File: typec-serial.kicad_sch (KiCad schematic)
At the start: 16 parts, among them IC1 NJM12888F33-TE1, J1 USB4085-GF-A_REVB, J2 Conn_01x04_Pin, U1 FT230XS

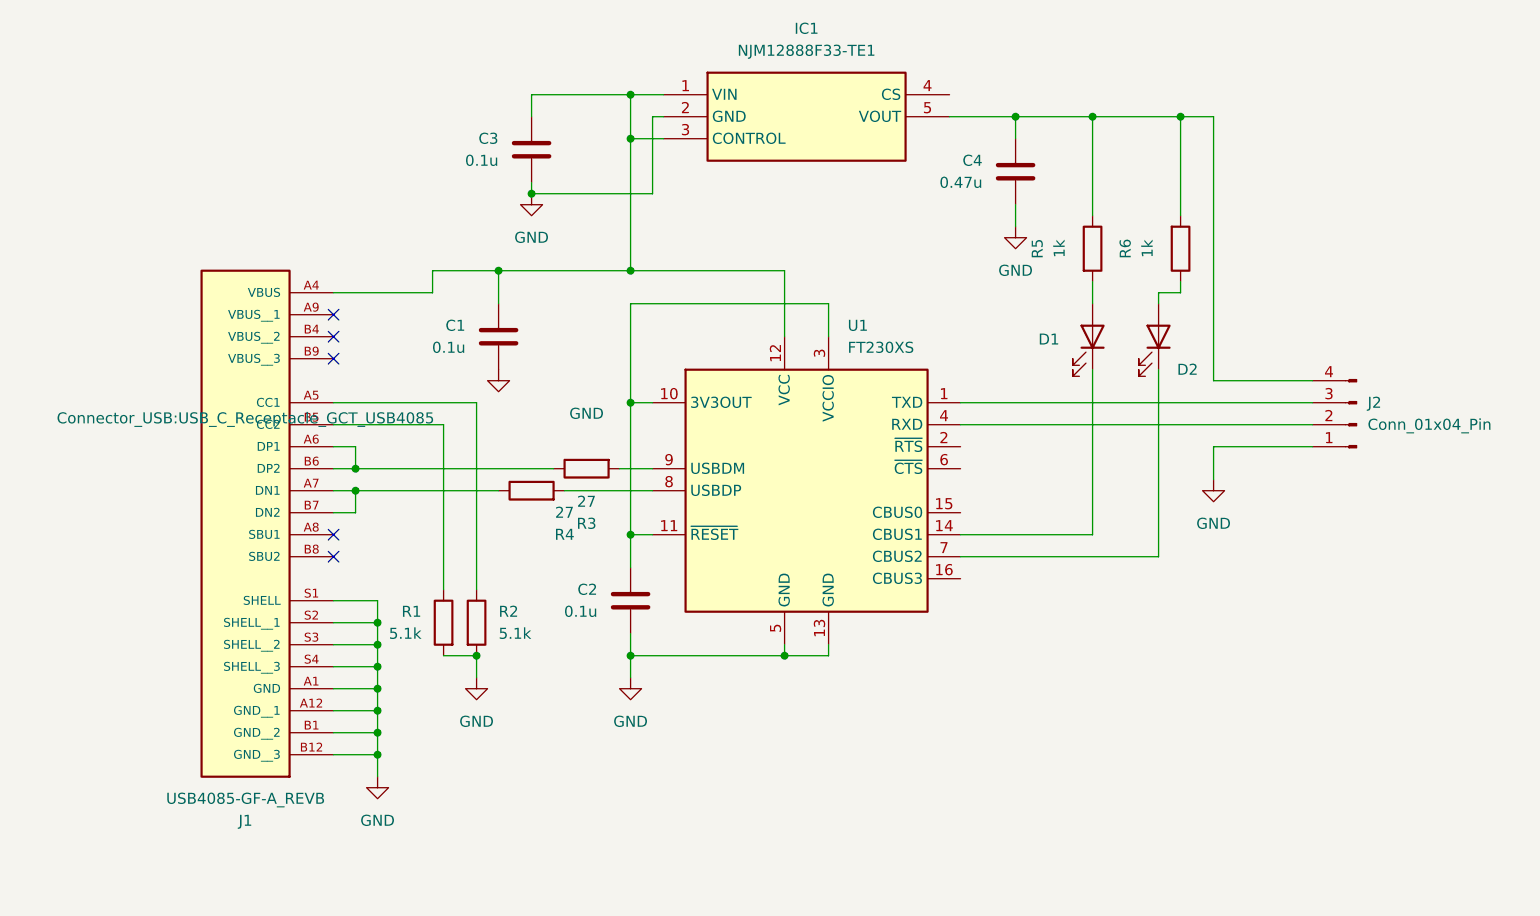
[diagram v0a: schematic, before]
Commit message: :fire: remove regulator
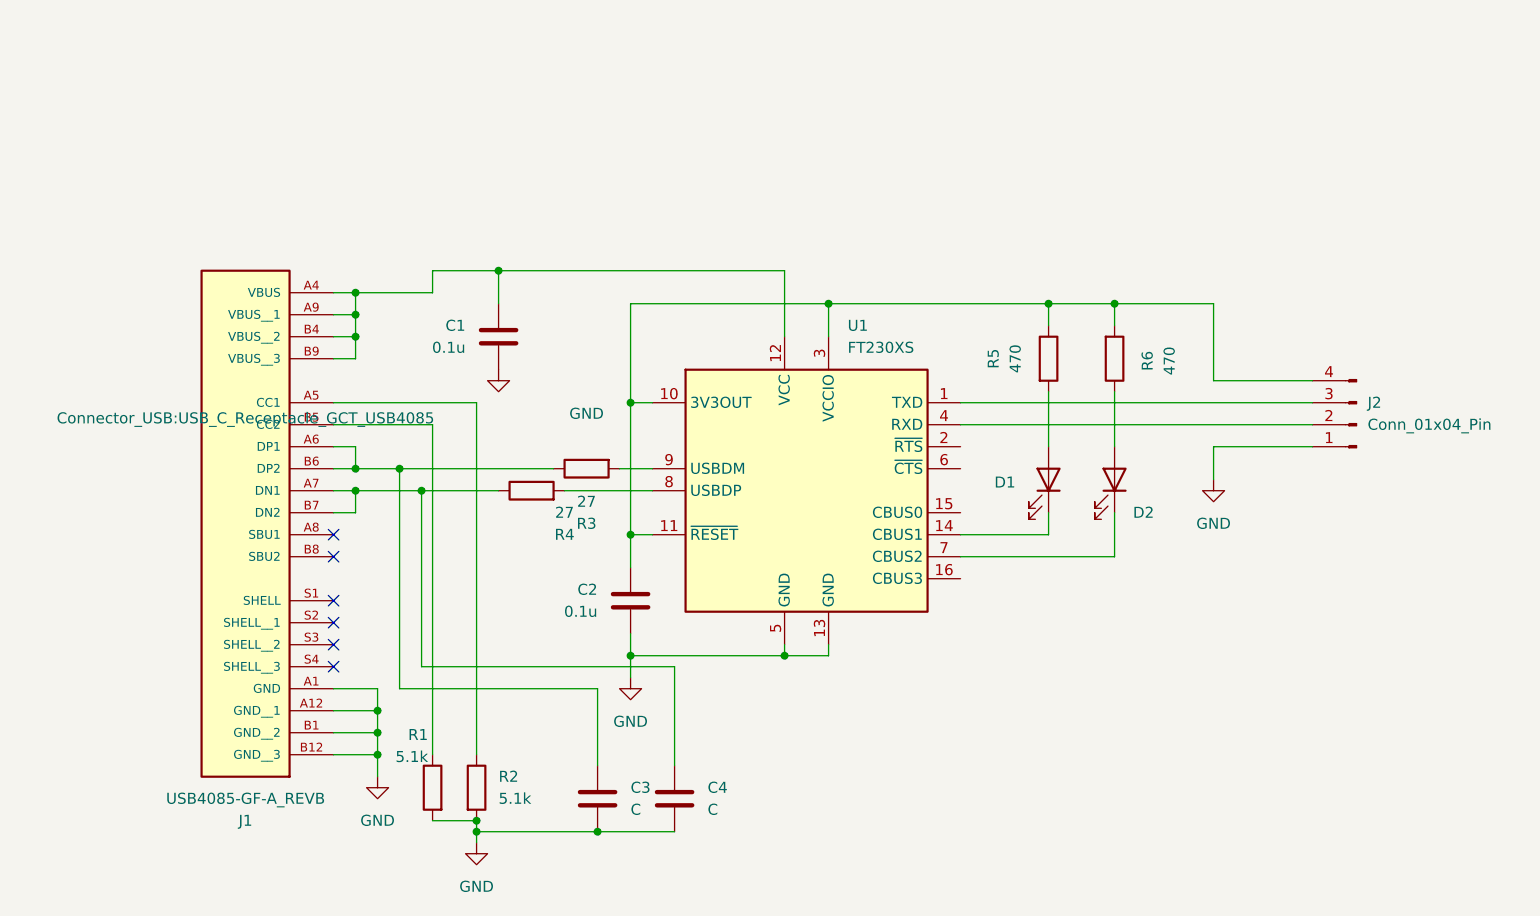
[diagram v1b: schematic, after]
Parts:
- removed IC1: NJM12888F33-TE1, footprints:PI-SOT-23-5-E-A_NMD, symbol NJM12888F33-TE1:NJM12888F33-TE1
- C3: value 0.1u -> C
- C4: value 0.47u -> C
- R5, R6: value 1k -> 470
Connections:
- net GND: now also C3.2, C4.2; no longer C3.1, C4.1, J1.S1 (SHELL), J1.S2 (SHELL__1), J1.S3 (SHELL__2), J1.S4 (SHELL__3)
- net at C2.2, U1.10 (3V3OUT), U1.11 (~{RESET})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: now also J2.4 (Pin_4), R5.1, R6.2
- net at C1.2, J1.A4 (VBUS), U1.12 (VCC): now also J1.A9 (VBUS__1), J1.B4 (VBUS__2), J1.B9 (VBUS__3); no longer C3.2
- net at J1.A7 (DN1), J1.B7 (DN2), R4.1: now also C4.1
- net at J1.A6 (DP1), J1.B6 (DP2), R3.1: now also C3.1
- no-connect marks 5 -> 6
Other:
- moved on the sheet: D1, D2, R1, R2, R5, R6
